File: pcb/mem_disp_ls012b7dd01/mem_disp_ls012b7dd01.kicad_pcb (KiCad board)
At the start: 2 copper layers, 11 x 41.5 mm, 3 parts, among them J1 Pin Header, J2 FCP Connector

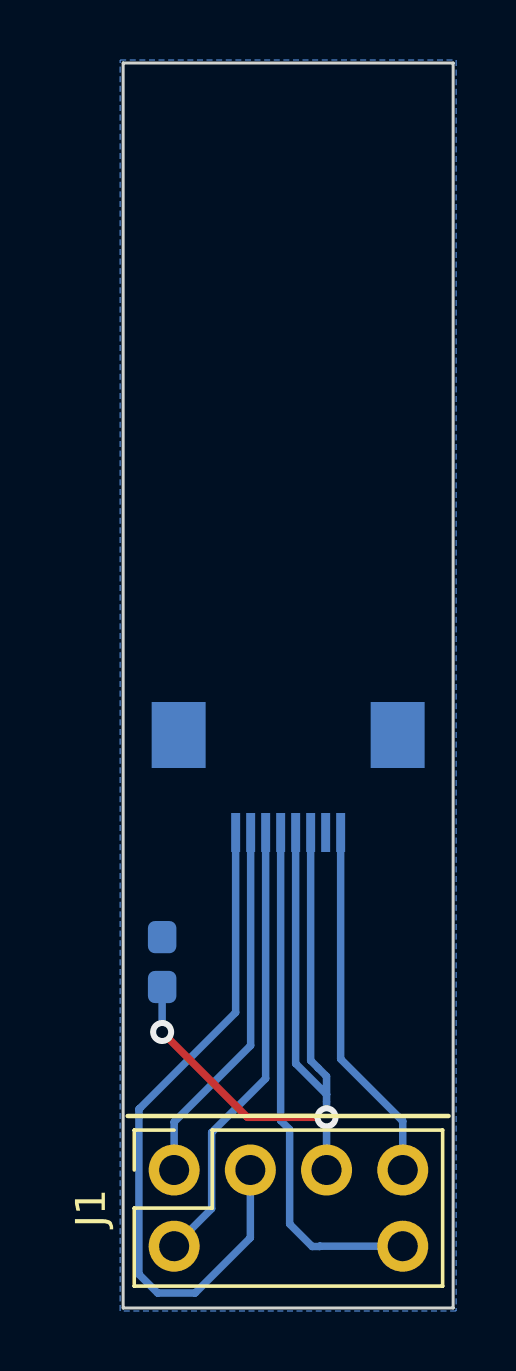
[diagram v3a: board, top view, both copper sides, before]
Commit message: Moved FPC connector up a little
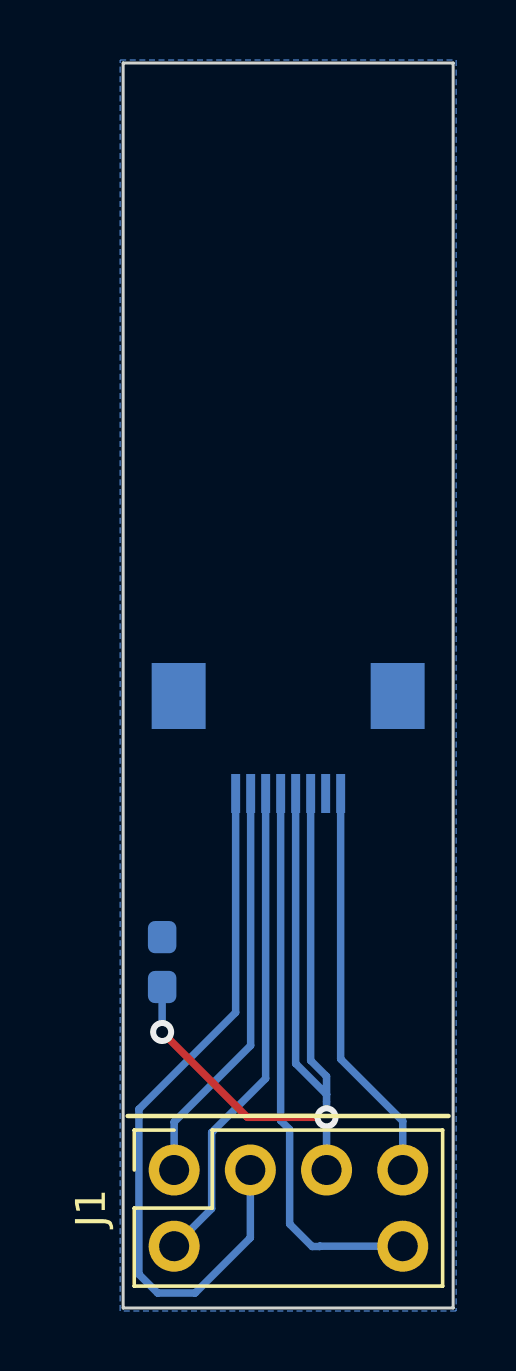
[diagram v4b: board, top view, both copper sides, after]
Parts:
- moved J2 1.30 mm to (55.5, 73.0)
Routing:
- net VDD: track 28.8 -> 31.4 mm
- net SI: track 12.3 -> 13.6 mm
- net SCS: track 15.1 -> 16.4 mm
- net SCLK: track 23.1 -> 24.4 mm
- net GND: track 12.1 -> 13.4 mm
- net EXTCOMIN: track 17.3 -> 18.6 mm
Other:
- board text added: "Shap Memory Disp. (LS012B7DD01) Breakout Board v0.3"
- board text removed: "Shap Memory Disp. (LS012B7DD01) Breakout Board v0.2"
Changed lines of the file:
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@@
   )
   (footprint "Connector_FFC-FPC:Hirose_FH12-8S-0.5SH_1x08-1MP_P0.50mm_Horizontal" (layer "B.Cu")
-    (at 55.5 74.3)
+    (at 55.5 73)
     (descr "Hirose FH12, FFC/FPC connector, FH12-8S-0.5SH, 8 Pins per row (https://www.hirose.com/product/en/products/FH12/FH12-24S-0.5SH(55)/), generated with kicad-footprint-generator")
     (tags "connector Hirose FH12 horizontal")
@@
   (gr_line (start 61 92) (end 61 50.5) (layer "Edge.Cuts") (width 0.1))
   (gr_line (start 50 92) (end 61 92) (layer "Edge.Cuts") (width 0.1))
-  (gr_text "Shap Memory Disp.\n(LS012B7DD01)\nBreakout Board v0.2" (at 55.6 53.4) (layer "B.SilkS")
+  (gr_text "Shap Memory Disp.\n(LS012B7DD01)\nBreakout Board v0.3" (at 55.6 53.4) (layer "B.SilkS")
     (effects (font (size 0.5 0.5) (thickness 0.125)) (justify mirror))
   )
@@
   )
   (dimension (type aligned) (layer "Cmts.User")
-    (pts (xy 56.05 50.45) (xy 56.05 72.95))
-    (height -11.2)
-    (gr_text "22.50 mm (Cable Len)" (at 66.1 61.7 90) (layer "Cmts.User")
+    (pts (xy 56.05 50.475) (xy 56.05 72.475))
+    (height -11.22525)
+    (gr_text "22.00 mm (Cable Len)" (at 66.12525 61.475 90) (layer "Cmts.User")
       (effects (font (size 1 1) (thickness 0.15)) (justify mirror))
     )
@@
   (via (at 51.3 82.8) (size 0.8) (drill 0.4) (layers "F.Cu" "B.Cu") (net 1))
   (via (at 56.78 85.645) (size 0.8) (drill 0.4) (layers "F.Cu" "B.Cu") (net 1))
+  (segment (start 55.75 83.85) (end 55.75 74.85) (width 0.25) (layer "B.Cu") (net 1))
   (segment (start 56.78 85.645) (end 56.78 85.13) (width 0.25) (layer "B.Cu") (net 1))
-  (segment (start 55.75 83.85) (end 56.78 84.88) (width 0.25) (layer "B.Cu") (net 1))
+  (segment (start 56.78 85.75) (end 56.78 85.645) (width 0.25) (layer "B.Cu") (net 1))
+  (segment (start 56.78 84.88) (end 55.75 83.85) (width 0.25) (layer "B.Cu") (net 1))
+  (segment (start 51.3 82.8) (end 51.3 81.3) (width 0.25) (layer "B.Cu") (net 1))
+  (segment (start 56.25 83.75) (end 56.25 74.85) (width 0.25) (layer "B.Cu") (net 1))
+  (segment (start 56.78 85.75) (end 56.78 87.4) (width 0.25) (layer "B.Cu") (net 1))
   (segment (start 56.78 84.88) (end 56.78 84.28) (width 0.25) (layer "B.Cu") (net 1))
-  (segment (start 56.78 85.75) (end 56.78 85.645) (width 0.25) (layer "B.Cu") (net 1))
-  (segment (start 51.3 82.8) (end 51.3 81.3) (width 0.25) (layer "B.Cu") (net 1))
-  (segment (start 55.75 76.15) (end 55.75 83.85) (width 0.25) (layer "B.Cu") (net 1))
-  (segment (start 56.78 84.28) (end 56.5 84) (width 0.25) (layer "B.Cu") (net 1))
-  (segment (start 56.78 85.75) (end 56.78 87.4) (width 0.25) (layer "B.Cu") (net 1))
-  (segment (start 56.25 83.75) (end 56.25 76.15) (width 0.25) (layer "B.Cu") (net 1))
-  (segment (start 56.5 84) (end 56.25 83.75) (width 0.25) (layer "B.Cu") (net 1))
+  (segment (start 56.78 84.28) (end 56.25 83.75) (width 0.25) (layer "B.Cu") (net 1))
   (segment (start 56.78 85.13) (end 56.78 84.88) (width 0.25) (layer "B.Cu") (net 1))
-  (segment (start 59.32 85.77) (end 59.275 85.725) (width 0.25) (layer "B.Cu") (net 2))
-  (segment (start 59.275 85.725) (end 57.25 83.7) (width 0.25) (layer "B.Cu") (net 2))
+  (segment (start 59.32 85.77) (end 57.25 83.7) (width 0.25) (layer "B.Cu") (net 2))
+  (segment (start 57.25 83.7) (end 57.25 74.85) (width 0.25) (layer "B.Cu") (net 2))
   (segment (start 59.32 87.4) (end 59.32 85.77) (width 0.25) (layer "B.Cu") (net 2))
-  (segment (start 57.25 83.7) (end 57.25 76.15) (width 0.25) (layer "B.Cu") (net 2))
+  (segment (start 54.25 83.25) (end 54.25 74.85) (width 0.25) (layer "B.Cu") (net 3))
   (segment (start 51.7 87.4) (end 51.7 85.8) (width 0.25) (layer "B.Cu") (net 3))
   (segment (start 51.7 85.8) (end 54.25 83.25) (width 0.25) (layer "B.Cu") (net 3))
-  (segment (start 54.25 83.25) (end 54.25 76.15) (width 0.25) (layer "B.Cu") (net 3))
+  (segment (start 54.24 87.4) (end 54.24 89.66) (width 0.25) (layer "B.Cu") (net 4))
+  (segment (start 52.4 91.5) (end 51.15 91.5) (width 0.25) (layer "B.Cu") (net 4))
+  (segment (start 53.75 82.15) (end 53.75 74.85) (width 0.25) (layer "B.Cu") (net 4))
+  (segment (start 50.525489 85.374511) (end 53.75 82.15) (width 0.25) (layer "B.Cu") (net 4))
+  (segment (start 51.15 91.5) (end 50.525489 90.875489) (width 0.25) (layer "B.Cu") (net 4))
   (segment (start 54.24 89.66) (end 52.4 91.5) (width 0.25) (layer "B.Cu") (net 4))
-  (segment (start 54.24 87.4) (end 54.24 89.66) (width 0.25) (layer "B.Cu") (net 4))
-  (segment (start 53.75 82.15) (end 53.75 76.15) (width 0.25) (layer "B.Cu") (net 4))
-  (segment (start 51.15 91.5) (end 50.525489 90.875489) (width 0.25) (layer "B.Cu") (net 4))
-  (segment (start 52.4 91.5) (end 51.15 91.5) (width 0.25) (layer "B.Cu") (net 4))
   (segment (start 50.525489 90.875489) (end 50.525489 85.374511) (width 0.25) (layer "B.Cu") (net 4))
-  (segment (start 50.55 85.35) (end 53.75 82.15) (width 0.25) (layer "B.Cu") (net 4))
-  (segment (start 50.525489 85.374511) (end 50.55 85.35) (width 0.25) (layer "B.Cu") (net 4))
   (segment (start 52.95 88.69) (end 52.95 86.15) (width 0.25) (layer "B.Cu") (net 5))
   (segment (start 52.95 86.15) (end 54.75 84.35) (width 0.25) (layer "B.Cu") (net 5))
-  (segment (start 54.75 84.35) (end 54.75 76.15) (width 0.25) (layer "B.Cu") (net 5))
   (segment (start 51.7 89.94) (end 52.95 88.69) (width 0.25) (layer "B.Cu") (net 5))
+  (segment (start 54.75 84.35) (end 54.75 74.85) (width 0.25) (layer "B.Cu") (net 5))
   (segment (start 59.32 89.94) (end 56.56 89.94) (width 0.25) (layer "B.Cu") (net 6))
-  (segment (start 55.25 85.75) (end 55.25 76.15) (width 0.25) (layer "B.Cu") (net 6))
+  (segment (start 55.55 86.05) (end 55.25 85.75) (width 0.25) (layer "B.Cu") (net 6))
+  (segment (start 55.25 85.75) (end 55.25 74.85) (width 0.25) (layer "B.Cu") (net 6))
+  (segment (start 56.56 89.94) (end 56.55 89.95) (width 0.25) (layer "B.Cu") (net 6))
   (segment (start 55.55 89.2) (end 55.55 86.05) (width 0.25) (layer "B.Cu") (net 6))
   (segment (start 56.55 89.95) (end 56.3 89.95) (width 0.25) (layer "B.Cu") (net 6))
   (segment (start 56.3 89.95) (end 55.55 89.2) (width 0.25) (layer "B.Cu") (net 6))
-  (segment (start 55.55 86.05) (end 55.25 85.75) (width 0.25) (layer "B.Cu") (net 6))
-  (segment (start 56.56 89.94) (end 56.55 89.95) (width 0.25) (layer "B.Cu") (net 6))
   (zone (net 2) (net_name "GND") (layer "B.Cu") (hatch edge 0.508)
     (connect_pads (clearance 0.508))
